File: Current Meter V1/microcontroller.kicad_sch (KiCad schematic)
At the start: 1 part

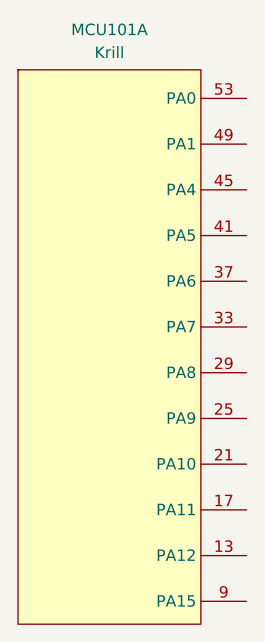
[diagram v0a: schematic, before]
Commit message: microcontroller pin renamed
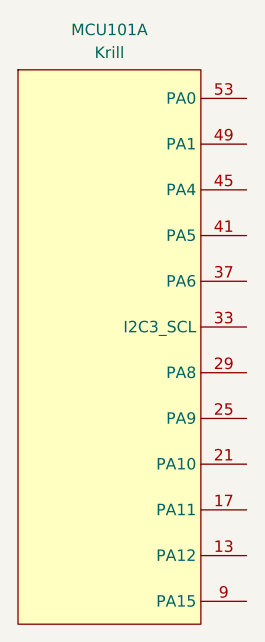
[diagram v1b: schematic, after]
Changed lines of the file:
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@@
 		)
 		(pin "33"
+			(alternate "I2C3_SCL")
 		)
 		(pin "16"
